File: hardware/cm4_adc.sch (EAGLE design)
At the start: 16 parts, among them J2 PJ-102A, Q1 2N7002, Q2 2.5A/30V/105mΩ, U1 ADT7420UCPZ-RL7

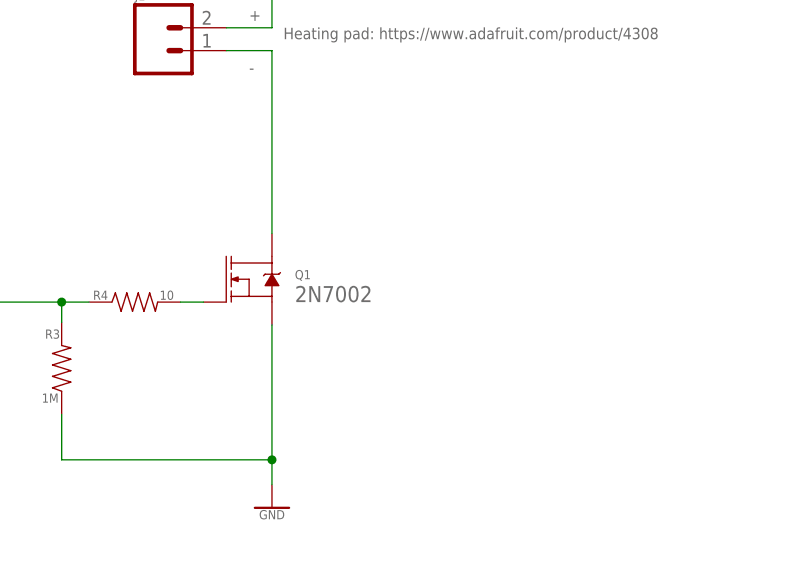
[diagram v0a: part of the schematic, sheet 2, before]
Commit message: Major file changes
Changes to Schematic, Part number updates etc.
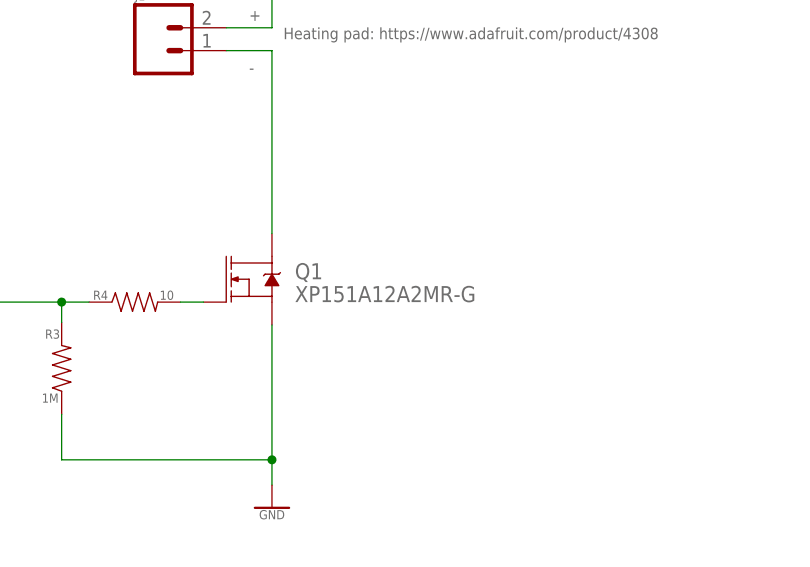
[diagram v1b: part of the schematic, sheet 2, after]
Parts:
- Q1: value 2N7002 -> XP151A12A2MR-G
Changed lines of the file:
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@@
 <part name="R1" library="SparkFun-Resistors" library_urn="urn:adsk.eagle:library:532" deviceset="2.2KOHM" device="-0603-1/10W-1%" package3d_urn="urn:adsk.eagle:package:39650/1" value="2.2k"/>
 <part name="R2" library="SparkFun-Resistors" library_urn="urn:adsk.eagle:library:532" deviceset="2.2KOHM" device="-0603-1/10W-1%" package3d_urn="urn:adsk.eagle:package:39650/1" value="2.2k"/>
-<part name="Q1" library="SparkFun-DiscreteSemi" library_urn="urn:adsk.eagle:library:514" deviceset="MOSFET-NCH" device="-2N7002PW" package3d_urn="urn:adsk.eagle:package:38456/1" value="2N7002"/>
+<part name="Q1" library="SparkFun-DiscreteSemi" library_urn="urn:adsk.eagle:library:514" deviceset="MOSFET-NCH" device="-2N7002PW" package3d_urn="urn:adsk.eagle:package:38456/1" value="XP151A12A2MR-G"/>
 <part name="GND6" library="SparkFun-PowerSymbols" library_urn="urn:adsk.eagle:library:530" deviceset="GND" device=""/>
 <part name="R3" library="SparkFun-Resistors" library_urn="urn:adsk.eagle:library:532" deviceset="1MOHM" device="-0603-1/4W-5%" package3d_urn="urn:adsk.eagle:package:39650/1" value="1M"/>
@@
 </instance>
 <instance part="Q1" gate="NMOS" x="195.58" y="119.38" smashed="yes">
-<attribute name="NAME" x="200.66" y="119.38" size="1.016" layer="95" font="vector" ratio="20"/>
+<attribute name="NAME" x="200.66" y="119.38" size="1.778" layer="95" font="vector" ratio="20"/>
 <attribute name="VALUE" x="200.66" y="116.84" size="1.778" layer="96" font="vector" ratio="20"/>
 </instance>
